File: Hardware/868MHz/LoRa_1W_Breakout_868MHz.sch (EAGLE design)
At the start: 26 parts, among them U4 E19-915M30S

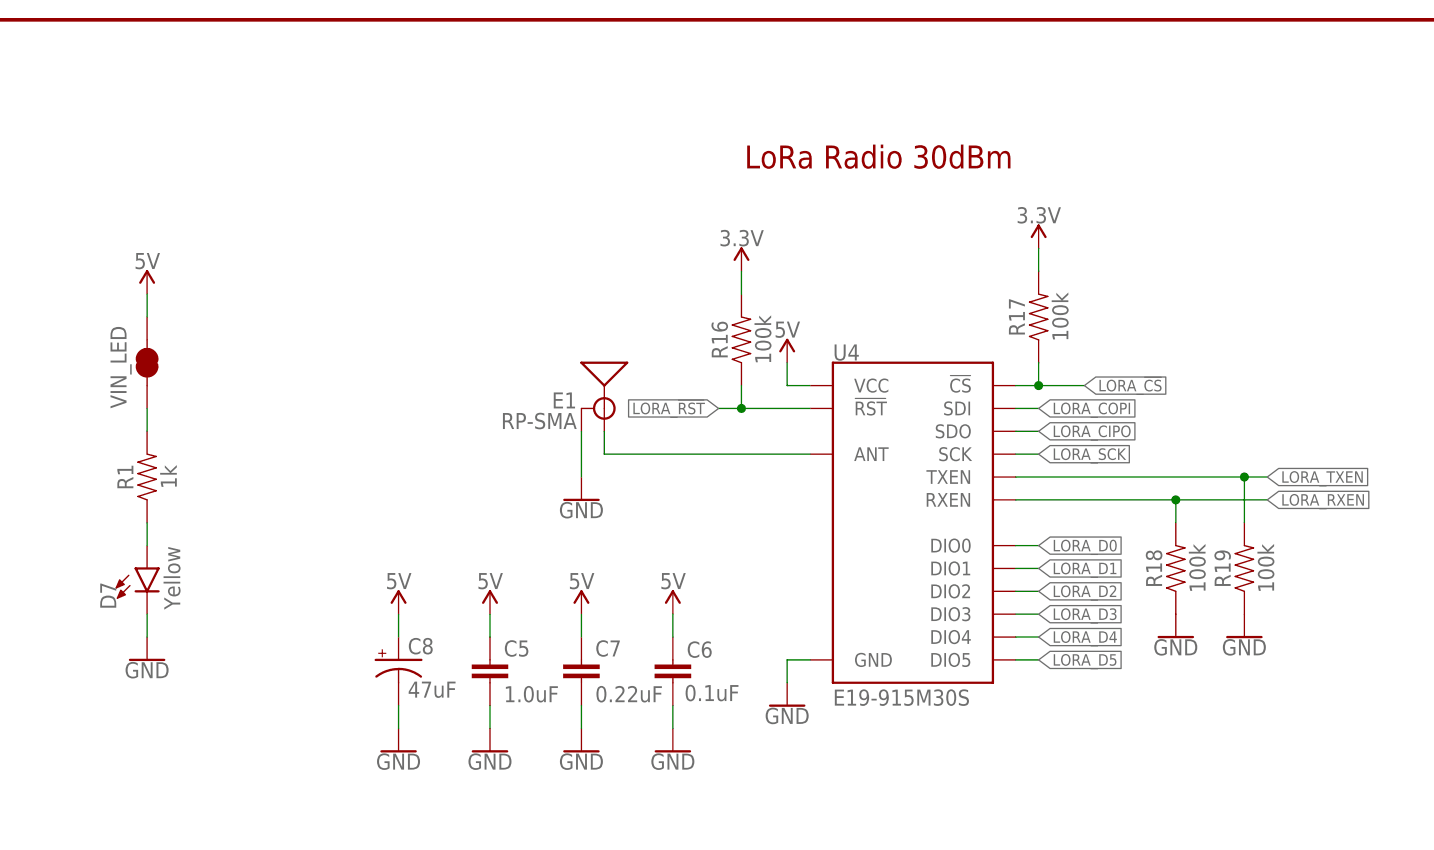
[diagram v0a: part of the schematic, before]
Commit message: Add 433 and 868
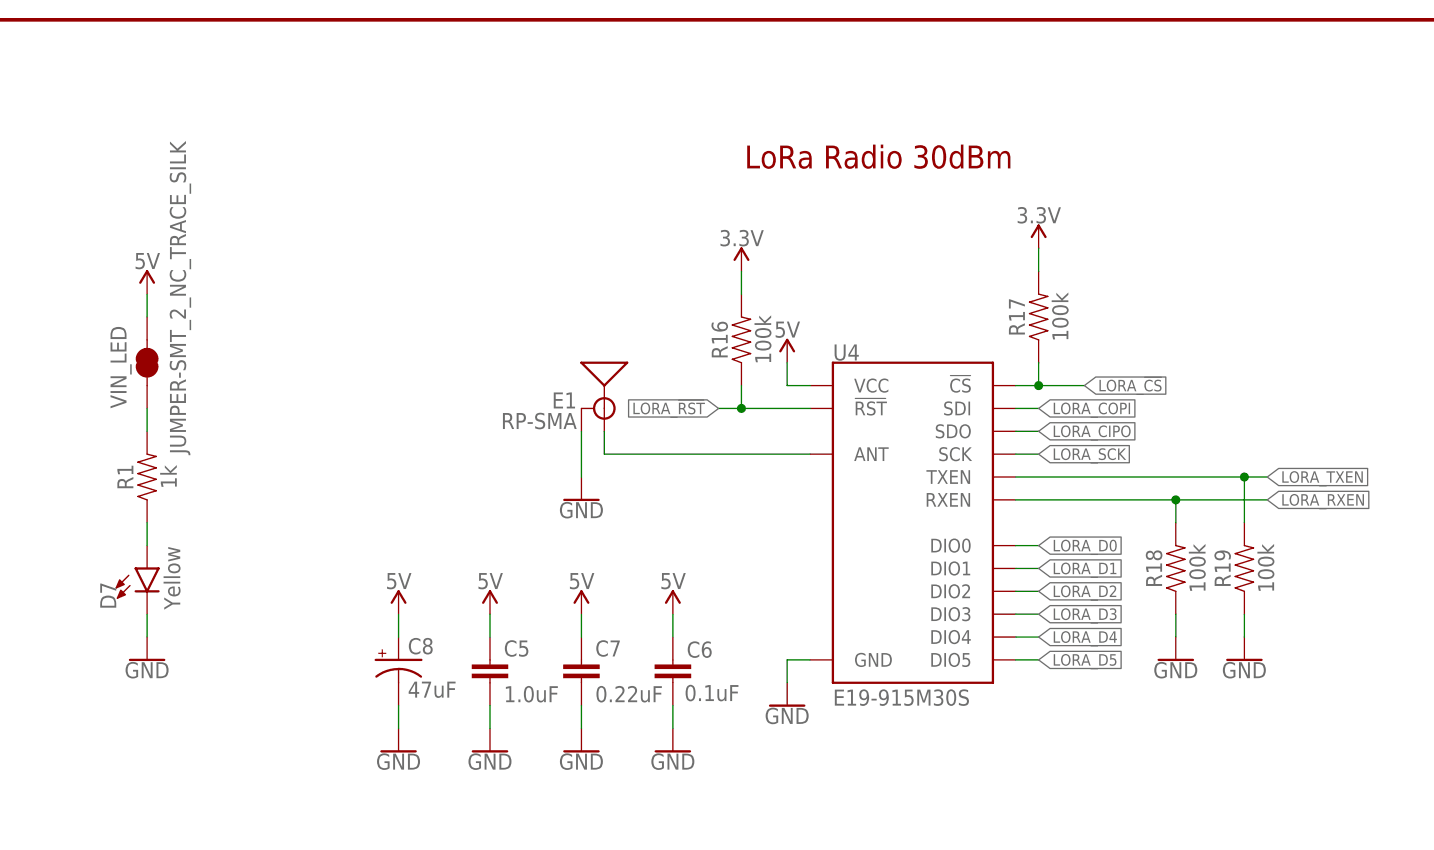
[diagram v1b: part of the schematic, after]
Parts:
- U4: device SparkFun-RF:E19-915MS1W -> SparkFun-RF:LORA-E19868MHZ
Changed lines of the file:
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@@
 <part name="GND16" library="SparkFun-PowerSymbols" deviceset="GND" device=""/>
 <part name="GND24" library="SparkFun-PowerSymbols" deviceset="GND" device=""/>
-<part name="VIN_LED" library="SparkFun-Jumpers" deviceset="JUMPER-SMT_2_NC_TRACE" device="_SILK" package3d_urn="urn:adsk.eagle:package:39281/1" value=""/>
+<part name="VIN_LED" library="SparkFun-Jumpers" deviceset="JUMPER-SMT_2_NC_TRACE" device="_SILK" package3d_urn="urn:adsk.eagle:package:39281/1" value="JUMPER-SMT_2_NC_TRACE_SILK"/>
 <part name="D7" library="SparkFun-LED" deviceset="LED-YELLOW" device="0603" value="Yellow"/>
 <part name="GND28" library="SparkFun-PowerSymbols" deviceset="GND" device=""/>
 <part name="SUPPLY8" library="SparkFun-PowerSymbols" deviceset="5V" device=""/>
 <part name="GND31" library="SparkFun-PowerSymbols" deviceset="GND" device=""/>
-<part name="U4" library="SparkFun-RF" deviceset="E19-915MS1W" device="" value="E19-915M30S"/>
+<part name="U4" library="SparkFun-RF" deviceset="LORA-E19" device="868MHZ" value="E19-915M30S"/>
 <part name="R16" library="SparkFun-Resistors" deviceset="100KOHM" device="-0603-1/10W-1%" value="100k"/>
 <part name="SUPPLY12" library="SparkFun-PowerSymbols" deviceset="3.3V" device=""/>
@@
 <attribute name="VALUE" x="166.624" y="124.46" size="1.778" layer="96" font="vector" rot="R90" align="top-center"/>
 </instance>
-<instance part="GND33" gate="1" x="157.48" y="116.84" smashed="yes">
-<attribute name="VALUE" x="157.48" y="116.586" size="1.778" layer="96" align="top-center"/>
-</instance>
-<instance part="GND34" gate="1" x="165.1" y="116.84" smashed="yes">
-<attribute name="VALUE" x="165.1" y="116.586" size="1.778" layer="96" align="top-center"/>
+<instance part="GND33" gate="1" x="157.48" y="114.3" smashed="yes">
+<attribute name="VALUE" x="157.48" y="114.046" size="1.778" layer="96" align="top-center"/>
+</instance>
+<instance part="GND34" gate="1" x="165.1" y="114.3" smashed="yes">
+<attribute name="VALUE" x="165.1" y="114.046" size="1.778" layer="96" align="top-center"/>
 </instance>
 <instance part="SUPPLY2" gate="G$1" x="101.6" y="119.38" smashed="yes">
@@
 <pinref part="R18" gate="G$1" pin="1"/>
 <pinref part="GND33" gate="1" pin="GND"/>
+<wire x1="157.48" y1="116.84" x2="157.48" y2="119.38" width="0.1524" layer="91"/>
 </segment>
 <segment>
 <pinref part="R19" gate="G$1" pin="1"/>
 <pinref part="GND34" gate="1" pin="GND"/>
-</segment>
-<segment>
+<wire x1="165.1" y1="116.84" x2="165.1" y2="119.38" width="0.1524" layer="91"/>
+</segment>
+<segment>

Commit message: Update schematics
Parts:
- U4: value E19-915M30S -> E19-868M30S
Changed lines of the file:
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@@
 <part name="GND16" library="SparkFun-PowerSymbols" deviceset="GND" device=""/>
 <part name="GND24" library="SparkFun-PowerSymbols" deviceset="GND" device=""/>
-<part name="VIN_LED" library="SparkFun-Jumpers" deviceset="JUMPER-SMT_2_NC_TRACE" device="_SILK" package3d_urn="urn:adsk.eagle:package:39281/1" value="JUMPER-SMT_2_NC_TRACE_SILK"/>
+<part name="VIN_LED" library="SparkFun-Jumpers" deviceset="JUMPER-SMT_2_NC_TRACE" device="_SILK" package3d_urn="urn:adsk.eagle:package:39281/1" value=""/>
 <part name="D7" library="SparkFun-LED" deviceset="LED-YELLOW" device="0603" value="Yellow"/>
 <part name="GND28" library="SparkFun-PowerSymbols" deviceset="GND" device=""/>
 <part name="SUPPLY8" library="SparkFun-PowerSymbols" deviceset="5V" device=""/>
 <part name="GND31" library="SparkFun-PowerSymbols" deviceset="GND" device=""/>
-<part name="U4" library="SparkFun-RF" deviceset="LORA-E19" device="868MHZ" value="E19-915M30S"/>
+<part name="U4" library="SparkFun-RF" deviceset="LORA-E19" device="868MHZ" value="E19-868M30S"/>
 <part name="R16" library="SparkFun-Resistors" deviceset="100KOHM" device="-0603-1/10W-1%" value="100k"/>
 <part name="SUPPLY12" library="SparkFun-PowerSymbols" deviceset="3.3V" device=""/>
